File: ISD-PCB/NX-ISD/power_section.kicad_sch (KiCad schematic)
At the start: 31 parts, among them P1 S2B-PH-SM4-TB, Q2 AO3401A, Q3 BC847W, U11 HYCW275-USBC24-050B, U13 RT9193-18GB, U15 USBLC6-2P6, U2 NCP167BMX330TBG, U8 BQ25170DSGR, U9 RT9193-28GB

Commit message: Updated v1p0 files
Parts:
- C11, C14: footprint Capacitor_SMD:C_0603_1608Metric -> Capacitor_SMD:C_0402_1005Metric
- C20, C21: value 1uF -> 1u
- C22: value 10uF -> 10u
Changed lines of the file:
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@@
 			)
 		)
-		(property "Value" "1uF"
+		(property "Value" "1u"
 			(at 67.31 128.2699 0)
 			(show_name no)
@@
 			)
 		)
-		(property "Footprint" "Capacitor_SMD:C_0603_1608Metric"
+		(property "Footprint" "Capacitor_SMD:C_0402_1005Metric"
 			(at 252.4252 57.15 0)
 			(hide yes)
@@
 			)
 		)
-		(property "Value" "1uF"
+		(property "Value" "1u"
 			(at 151.13 137.1599 0)
 			(show_name no)
@@
 			)
 		)
-		(property "Value" "10uF"
+		(property "Value" "10u"
 			(at 163.83 137.1599 0)
 			(show_name no)
@@
 			)
 		)
-		(property "Footprint" "Capacitor_SMD:C_0603_1608Metric"
+		(property "Footprint" "Capacitor_SMD:C_0402_1005Metric"
 			(at 183.8452 57.15 0)
 			(hide yes)

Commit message: Fixed: polarity of NPM Pmos
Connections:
- net VBAT: now also Q2.2 (S); no longer Q2.3 (D)
- net VN: now also Q2.3 (D); no longer Q2.2 (S)
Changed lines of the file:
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@@
 		(lib_id "Transistor_FET:AO3401A")
 		(at 237.49 138.43 0)
+		(mirror x)
 		(unit 1)
 		(body_style 1)
@@
 		(dnp no)
 		(property "Reference" "Q2"
-			(at 243.84 137.1599 0)
+			(at 243.84 139.7001 0)
 			(show_name no)
 			(do_not_autoplace no)
@@
 		)
 		(property "Value" "AO3401A"
-			(at 243.84 139.6999 0)
+			(at 243.84 137.1601 0)
 			(show_name no)
 			(do_not_autoplace no)
@@
 		)
 		(property "Footprint" "Package_TO_SOT_SMD:SOT-23"
-			(at 242.57 140.335 0)
+			(at 242.57 136.525 0)
 			(hide yes)
 			(show_name no)
@@
 		)
 		(property "Datasheet" "http://www.aosmd.com/pdfs/datasheet/AO3401A.pdf"
-			(at 242.57 142.24 0)
+			(at 242.57 134.62 0)
 			(hide yes)
 			(show_name no)

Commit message: v1p1 rework in progress
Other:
- note added: "-> Connects to 1S Lipo PKCELL 3.7 V, 1200 mAh"
- moved on the sheet: P1
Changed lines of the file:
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@@
 		)
 	)
+	(text "-> Connects to 1S Lipo\nPKCELL\n3.7 V, 1200 mAh"
+		(exclude_from_sim no)
+		(at 139.7 79.248 0)
+		(effects
+			(font
+				(size 1.27 1.27)
+			)
+			(justify right)
+		)
+	)
 	(text "[0603]"
 		(exclude_from_sim no)
@@
 	(wire
 		(pts
-			(xy 109.22 77.47) (xy 113.03 77.47)
+			(xy 104.14 77.47) (xy 100.33 77.47)
 		)
 		(stroke
@@
 	(wire
 		(pts
-			(xy 109.22 80.01) (xy 113.03 80.01)
+			(xy 104.14 80.01) (xy 100.33 80.01)
 		)
 		(stroke
@@
 	(wire
 		(pts
-			(xy 113.03 73.66) (xy 113.03 77.47)
+			(xy 100.33 73.66) (xy 100.33 77.47)
 		)
 		(stroke
@@
 	(wire
 		(pts
-			(xy 113.03 82.55) (xy 113.03 80.01)
+			(xy 100.33 82.55) (xy 100.33 80.01)
 		)
 		(stroke
@@
 	(symbol
 		(lib_id "power:GND")
-		(at 113.03 82.55 0)
+		(at 100.33 82.55 0)
+		(mirror y)
 		(unit 1)
 		(body_style 1)
@@
 		(fields_autoplaced yes)
 		(property "Reference" "#PWR013"
-			(at 113.03 88.9 0)
+			(at 100.33 88.9 0)
 			(hide yes)
 			(show_name no)
@@
 		)
 		(property "Value" "GND"
-			(at 113.03 87.63 0)
+			(at 100.33 87.63 0)
 			(show_name no)
 			(do_not_autoplace no)
@@
 		)
 		(property "Footprint" ""
-			(at 113.03 82.55 0)
+			(at 100.33 82.55 0)
 			(hide yes)
 			(show_name no)
@@
 		)
 		(property "Datasheet" ""
-			(at 113.03 82.55 0)
+			(at 100.33 82.55 0)
 			(hide yes)
 			(show_name no)
@@
 		)
 		(property "Description" "Power symbol creates a global label with name \"GND\" , ground"
-			(at 113.03 82.55 0)
+			(at 100.33 82.55 0)
 			(hide yes)
 			(show_name no)
@@
 	(symbol
 		(lib_id "S2B-PH-SM4-TB:S2B-PH-SM4-TB")
-		(at 104.14 78.74 0)
-		(mirror y)
+		(at 109.22 78.74 0)
 		(unit 1)
 		(body_style 1)
@@
 		(dnp no)
 		(property "Reference" "P1"
-			(at 101.346 73.66 0)
+			(at 112.014 73.66 0)
 			(show_name no)
 			(do_not_autoplace no)
@@
 		)
 		(property "Value" "S2B-PH-SM4-TB"
-			(at 110.236 84.836 0)
+			(at 103.124 84.836 0)
 			(show_name no)
 			(do_not_autoplace no)
@@
 		)
 		(property "Footprint" "Global Footprints:JST_S2B-PH-SM4-TB"
-			(at 104.14 78.74 0)
+			(at 109.22 78.74 0)
 			(hide yes)
 			(show_name no)
@@
 		)
 		(property "Datasheet" ""
-			(at 104.14 78.74 0)
+			(at 109.22 78.74 0)
 			(hide yes)
 			(show_name no)
@@
 		)
 		(property "Description" ""
-			(at 104.14 78.74 0)
+			(at 109.22 78.74 0)
 			(hide yes)
 			(show_name no)
@@
 		)
 		(property "MF" "JST Sales"
-			(at 104.14 78.74 0)
+			(at 109.22 78.74 0)
 			(hide yes)
 			(show_name no)
@@
 		)
 		(property "Description_1" "Connector Header Surface Mount, Right Angle 2 position 0.079 (2.00mm)"
-			(at 104.14 78.74 0)
+			(at 109.22 78.74 0)
 			(hide yes)
 			(show_name no)
@@
 		)
 		(property "Package" "None"
-			(at 104.14 78.74 0)
+			(at 109.22 78.74 0)
 			(hide yes)
 			(show_name no)
@@
 		)
 		(property "Price" "None"
-			(at 104.14 78.74 0)
+			(at 109.22 78.74 0)
 			(hide yes)
 			(show_name no)
@@
 		)
 		(property "Check_prices" "https://www.snapeda.com/parts/S2B-PH-SM4-TB/JST/view-part/?ref=eda"
-			(at 104.14 78.74 0)
+			(at 109.22 78.74 0)
 			(hide yes)
 			(show_name no)
@@
 		)
 		(property "SnapEDA_Link" "https://www.snapeda.com/parts/S2B-PH-SM4-TB/JST/view-part/?ref=snap"
-			(at 104.14 78.74 0)
+			(at 109.22 78.74 0)
 			(hide yes)
 			(show_name no)
@@
 		)
 		(property "MP" "S2B-PH-SM4-TB"
-			(at 104.14 78.74 0)
+			(at 109.22 78.74 0)
 			(hide yes)
 			(show_name no)
@@
 		)
 		(property "Availability" "In Stock"
-			(at 104.14 78.74 0)
+			(at 109.22 78.74 0)
 			(hide yes)
 			(show_name no)
@@
 		)
 		(property "MANUFACTURER" "JST"
-			(at 104.14 78.74 0)
+			(at 109.22 78.74 0)
 			(hide yes)
 			(show_name no)
@@
 	(symbol
 		(lib_id "power:VBUS")
-		(at 113.03 73.66 0)
+		(at 100.33 73.66 0)
+		(mirror y)
 		(unit 1)
 		(body_style 1)
@@
 		(fields_autoplaced yes)
 		(property "Reference" "#PWR0101"
-			(at 113.03 77.47 0)
+			(at 100.33 77.47 0)
 			(hide yes)
 			(show_name no)
@@
 		)
 		(property "Value" "VBAT"
-			(at 113.03 68.58 0)
+			(at 100.33 68.58 0)
 			(show_name no)
 			(do_not_autoplace no)
@@
 		)
 		(property "Footprint" ""
-			(at 113.03 73.66 0)
+			(at 100.33 73.66 0)
 			(hide yes)
 			(show_name no)
@@
 		)
 		(property "Datasheet" ""
-			(at 113.03 73.66 0)
+			(at 100.33 73.66 0)
 			(hide yes)
 			(show_name no)
@@
 		)
 		(property "Description" "Power symbol creates a global label with name \"VBUS\""
-			(at 113.03 73.66 0)
+			(at 100.33 73.66 0)
 			(hide yes)
 			(show_name no)

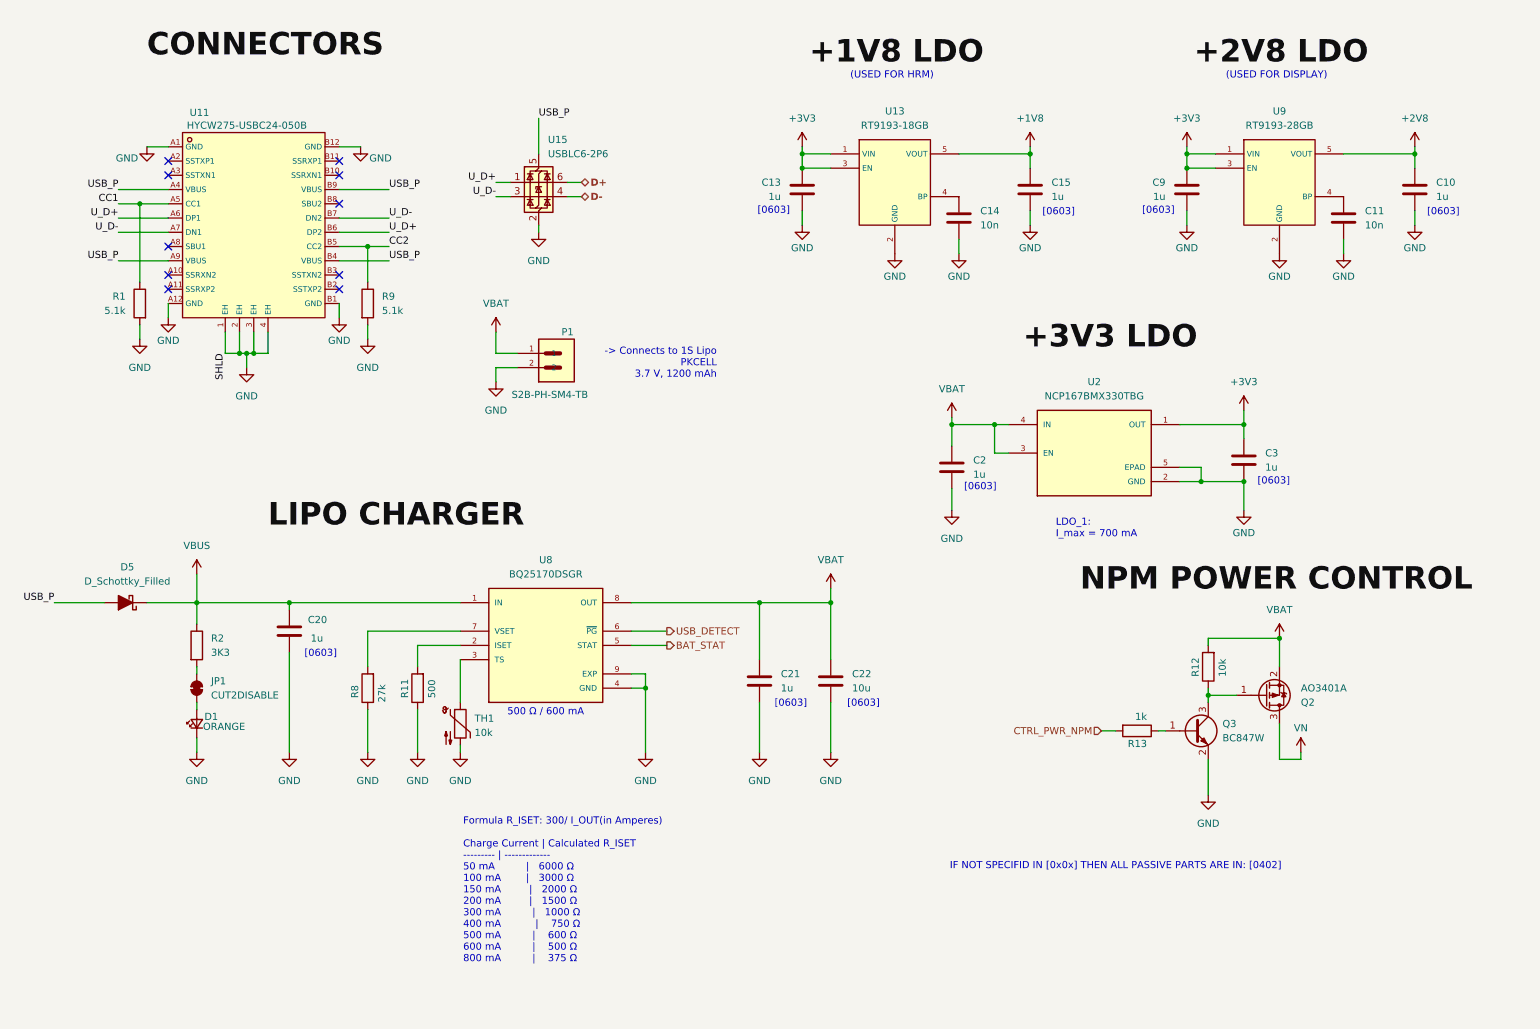
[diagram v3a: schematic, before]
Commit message: added software planed feature and progress on v1p1
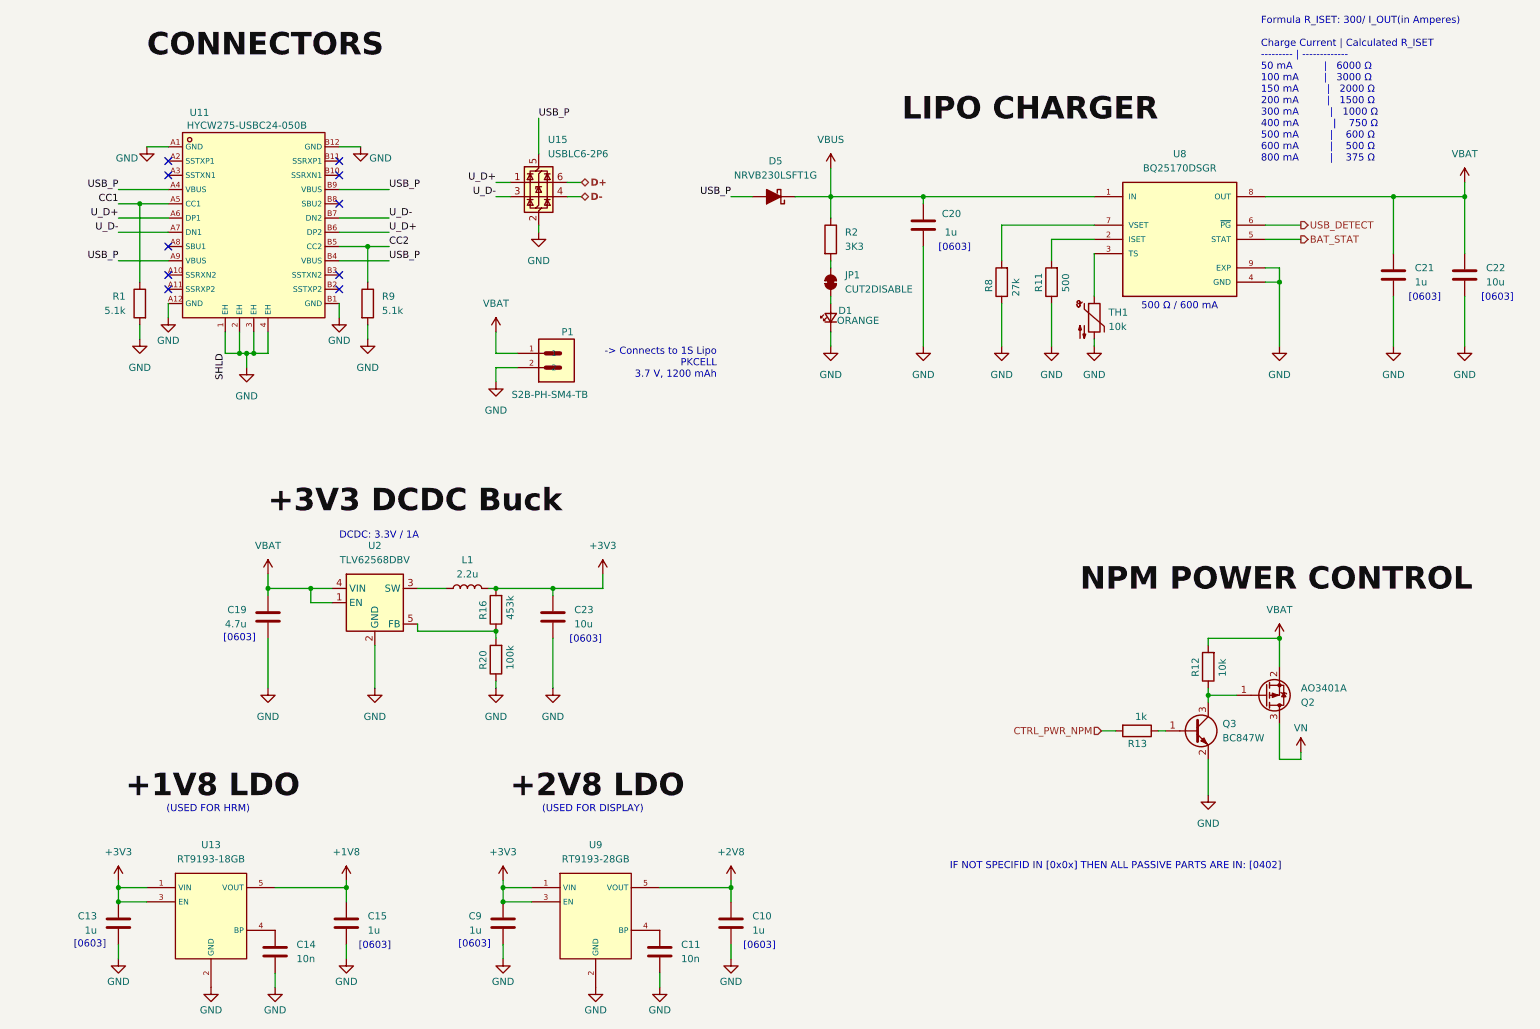
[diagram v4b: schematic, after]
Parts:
- removed C2, C3: 1u, Capacitor_SMD:C_0603_1608Metric, symbol Device:C
- removed U2: NCP167BMX330TBG, Global Footprints:VREG_NCP167BMX330TBG, symbol NCP167BMX330TBG:NCP167BMX330TBG
- added C19: 4.7u, Capacitor_SMD:C_0603_1608Metric, symbol Device:C
- added C23: 10u, Capacitor_SMD:C_0603_1608Metric, symbol Device:C
- added L1: 2.2u, Inductor_SMD:L_1206_3216Metric, symbol Device:L
- added R16: 453k, Resistor_SMD:R_0402_1005Metric, symbol Device:R
- added R20: 100k, Resistor_SMD:R_0402_1005Metric, symbol Device:R
- added U2: TLV62568DBV, Package_TO_SOT_SMD:SOT-23-5, symbol Regulator_Switching:TLV62568DBV
- D5: value D_Schottky_Filled -> NRVB230LSFT1G
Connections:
- net +3V3: now also C23.1, L1.2, R16.2
- net GND: now also C19.2, C23.2, R20.1, U2.2 (GND)
- net VBAT: now also C19.1, U2.1 (EN), U2.4 (VIN)
- new net: L1.1, U2.3 (SW)
- new net: R16.1, R20.2, U2.5 (FB)
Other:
- note added: "DCDC: 3.3V / 1A"
- note removed: "LDO_1: I_max = 700 mA"
- moved on the sheet: C10, C11, C13, C14, C15, C20, C21, C22, C9, D1, D5, JP1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

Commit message: v1p1 updates
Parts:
- L1: footprint Inductor_SMD:L_1206_3216Metric -> Inductor_SMD:L_1008_2520Metric
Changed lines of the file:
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@@
 			)
 		)
-		(property "Footprint" "Inductor_SMD:L_1206_3216Metric"
+		(property "Footprint" "Inductor_SMD:L_1008_2520Metric"
 			(at 95.25 119.38 0)
 			(hide yes)

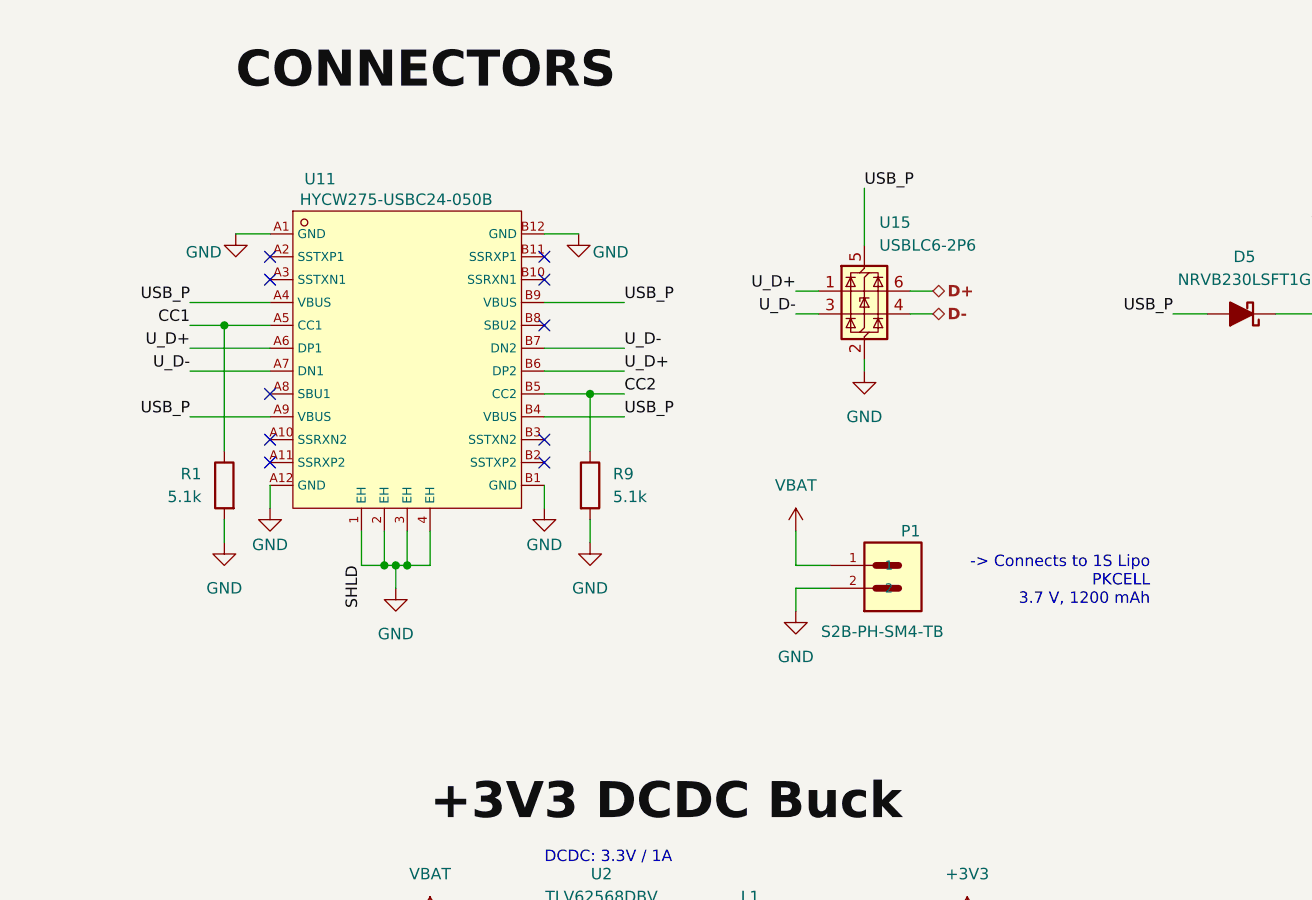
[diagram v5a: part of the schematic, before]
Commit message: new USBC plug and minor changes to ISD-Core
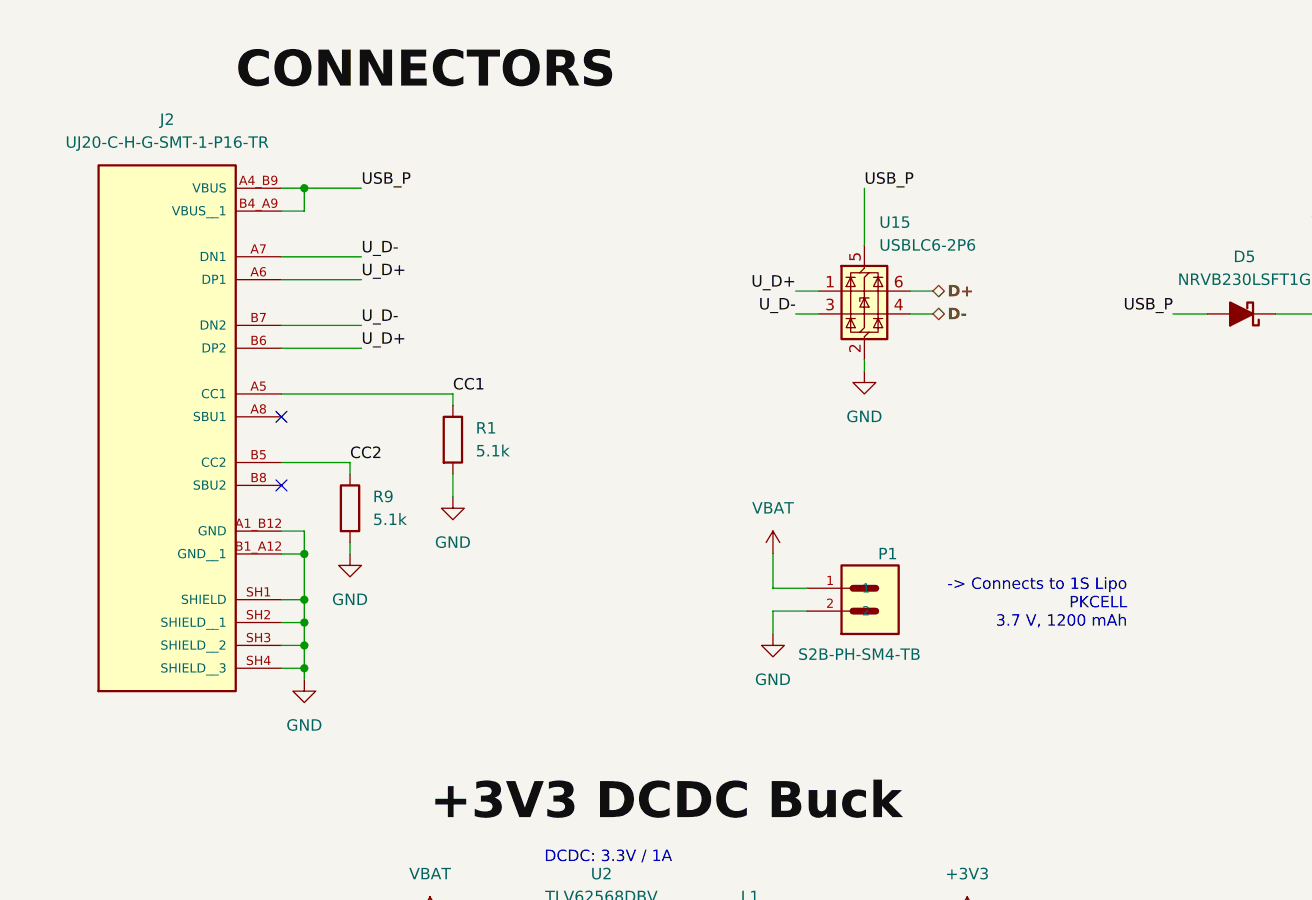
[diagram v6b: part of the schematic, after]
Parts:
- removed U11: HYCW275-USBC24-050B, Global Footprints:USB-C-SMD_HYCW275-USBC24-050B, symbol HYCW275-USBC24-050B:HYCW275-USBC24-050B
- added J2: UJ20-C-H-G-SMT-1-P16-TR, NX-AW-footprints:SAMESKY_UJ20-C-H-G-SMT-1-P16-TR, symbol UJ20-C-H-G-SMT-1-P16-TR:UJ20-C-H-G-SMT-1-P16-TR
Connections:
- net CC1: now also J2.A5 (CC1)
- net CC2: now also J2.B5 (CC2)
- net GND: now also J2.A1_B12 (GND), J2.B1_A12 (GND__1), J2.SH1 (SHIELD), J2.SH2 (SHIELD__1), J2.SH3 (SHIELD__2), J2.SH4 (SHIELD__3)
- net USB_P: now also J2.A4_B9 (VBUS), J2.B4_A9 (VBUS__1)
- net U_D+: now also J2.A6 (DP1), J2.B6 (DP2)
- net U_D-: now also J2.A7 (DN1), J2.B7 (DN2)
- no-connect marks 10 -> 2
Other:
- moved on the sheet: P1, R1, R9

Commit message: v1p3 major fix rework in progress
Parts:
- R11: value 500 -> 499
- R2: value 3K3 -> 499
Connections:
- net +3V3: now also R2.1
- net BAT_STAT: now also D1.1 (K)
- net GND: no longer D1.1 (K)
- net VBUS: no longer R2.1
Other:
- note added: "ATTENTION FOR L1: I HIGHLY RECOMMAND USING A SHIELDED COIL TO REDUCE EMI"
- note added: "Connects to 1S Lipo -> PKCELL 3.7 V, 1200 mAh"
- note removed: "-> Connects to 1S Lipo PKCELL 3.7 V, 1200 mAh"
- moved on the sheet: D1, JP1, L1, P1, R2, U15
